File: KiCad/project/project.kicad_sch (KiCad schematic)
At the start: 27 parts, among them P1 TerminalBlock 5P 5.0mm, U1 DRV8313PWPR

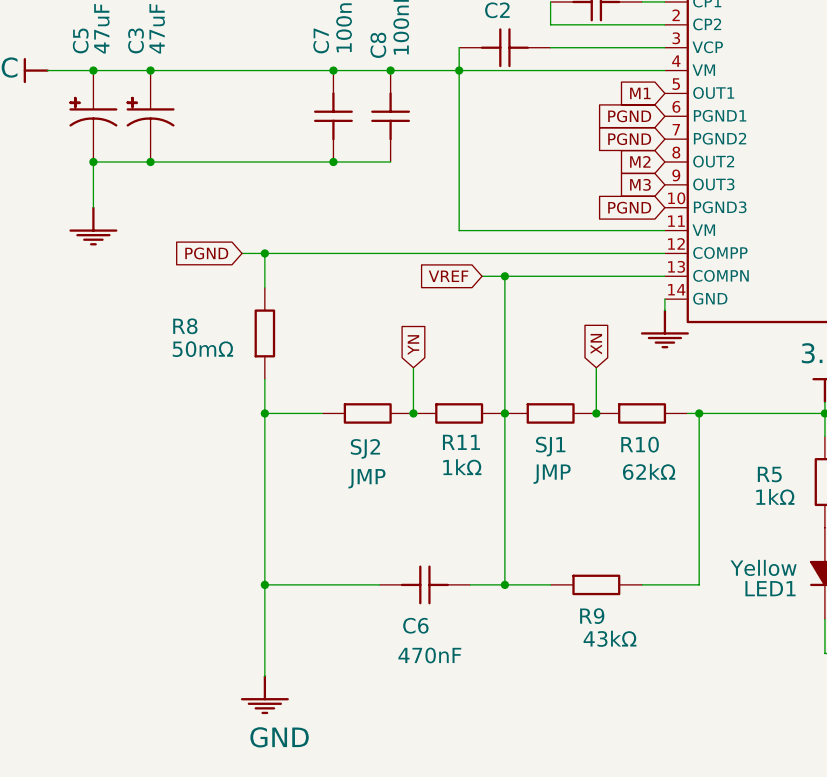
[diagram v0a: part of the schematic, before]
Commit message: Review manual layout; add power/GND/thermal improvements
Schematic: graphical-only relayout (R8/PGND-label moved, redundant GND
symbol added) — netlist verified byte-identical to prior commit; ERC 101->98.

PCB fixes & improvements:
- Re-ground U1's 8 EP thermal vias (Update-from-Schematic had stripped GND)
  and rename them to pad "29" so they survive every future sync.
- Add Power net class (0.6mm) for VCC/M1/M2/M3/PGND; widen the current-
  carrying runs 0.2->0.6mm with neck-down kept at the HTSSOP escape.
- Add F.Cu + B.Cu GND pours + 38 stitching vias (datasheet 10.1; lowers
  RthJA, better return paths/EMI).
- Extend EP thermal-via array 8->12 (6x2); add GND-return vias at the C7/C8
  VM decoupling caps.

Tooling/docs:
- check_design.py: gate hard on kicad-cli (authoritative for connectivity/
  clearance/shorts); demote KiCadRoutingTools checks to advisory (they false-
  positive on through-pad/off-anchor manual routing); re-baseline ERC to 98.
- Update CLAUDE.md + tools/README.md to match.

Verified: 0 error-severity DRC, 0 unconnected (kicad-cli), check_design PASS.
Manufacturing outputs (manufacturing/, images/) NOT regenerated — still stale.

Co-Authored-By: Claude Opus 4.8 (1M context) <noreply@anthropic.com>
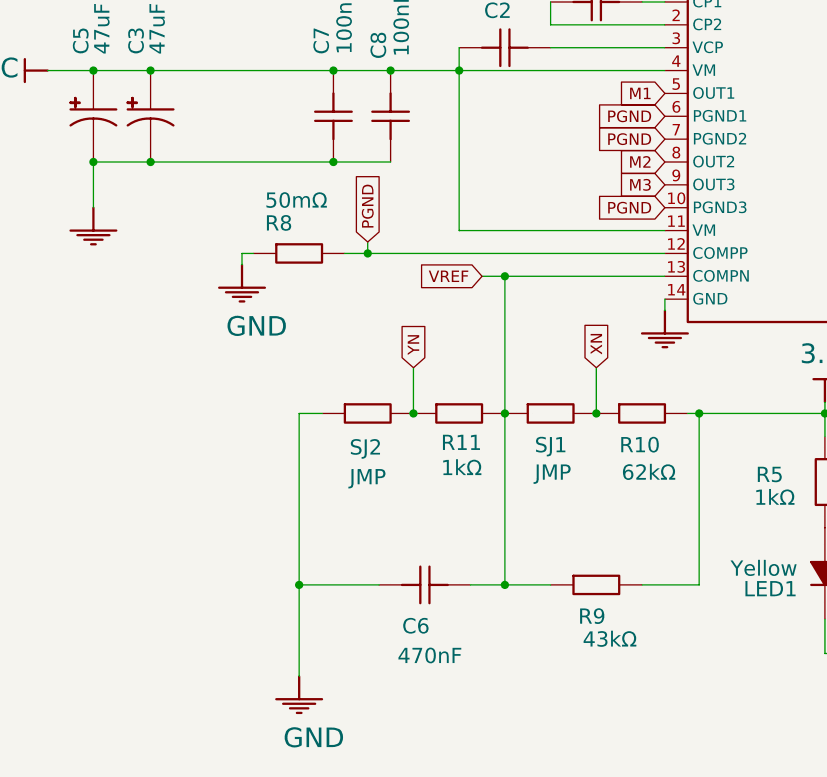
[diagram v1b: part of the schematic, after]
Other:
- moved on the sheet: R8

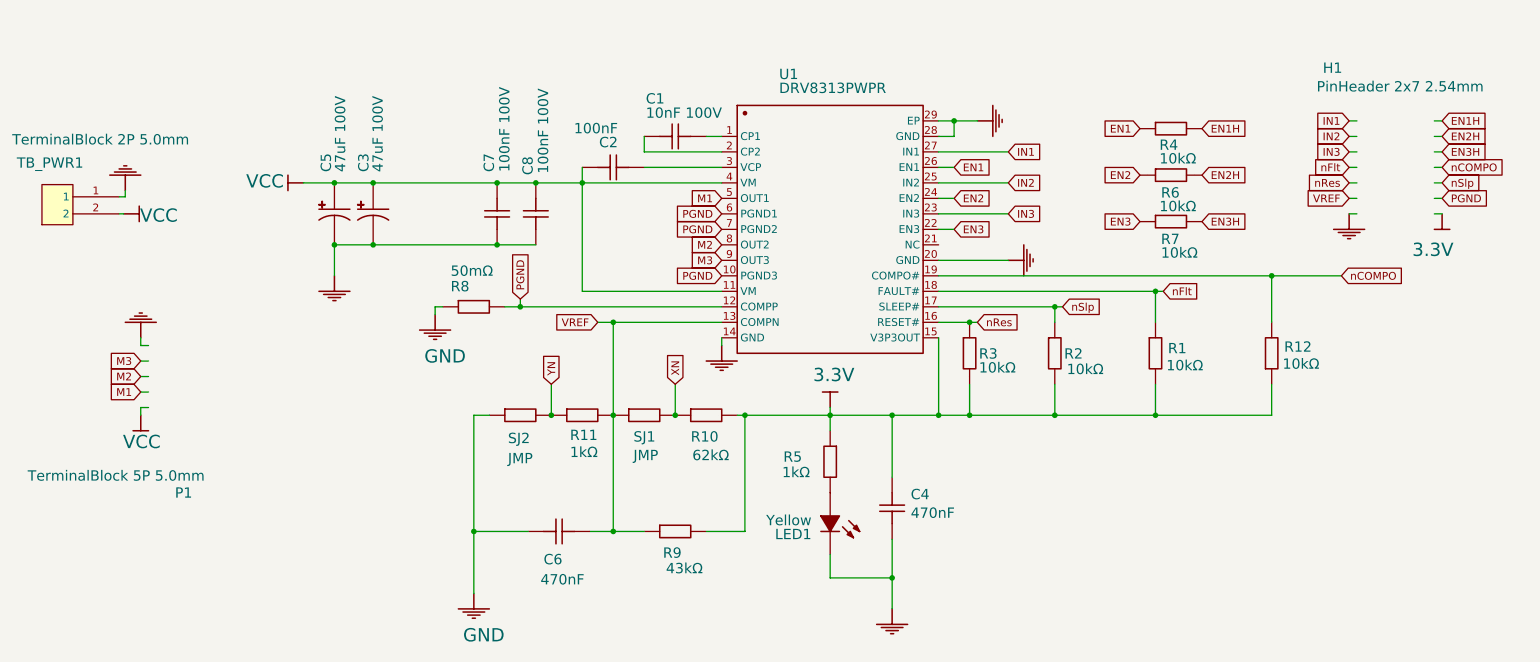
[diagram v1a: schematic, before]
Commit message: Swap simple passives to KiCad Device symbols; clear all ERC errors
Per user direction, move the simple passives off the EasyEDA-imported symbols
onto KiCad library symbols, and fix the schematic so ERC has zero errors.

- R1-R12 -> Device:R, ceramics -> Device:C, electrolytics C3/C5 ->
  Device:C_Polarized, SJ1/SJ2 -> Jumper:SolderJumper_2_Bridged. Removed the 9
  now-unused old EasyEDA passive lib_symbols. Kept U1 (no KiCad equivalent),
  H1/P1 (already generic), TB_PWR1.
- LED1 kept on its symbol (Device:LED numbers pin1=K, conflicting with the
  verified PCB pad1=anode) but its pins retyped input->passive.
- Added PWR_FLAG on VCC/GND/3.3V and a no-connect on U1.21.

Net-preserving: verified 28/28 netlist node-set parity vs the prior schematic
(re-stubbed 1.27mm where Device span 7.62 != old 10.16; jumper 10.16 exact).
kicad-skip mis-orders pin1/pin2 for some rotations, so kicad-cli netlist was
used as the oracle to detect and correct flipped parts.

ERC 98 (10 err/88 warn) -> 53 (0 err/53 warn); remaining are all import
artifacts (lib_symbol_issues/pin_to_pin/off-grid on the kept symbols).
Re-baselined check_design.py 98->53; updated tools/README.md + CLAUDE.md.
BOM unchanged; PCB untouched (only schematic.svg regenerated).

Co-Authored-By: Claude Opus 4.8 (1M context) <noreply@anthropic.com>
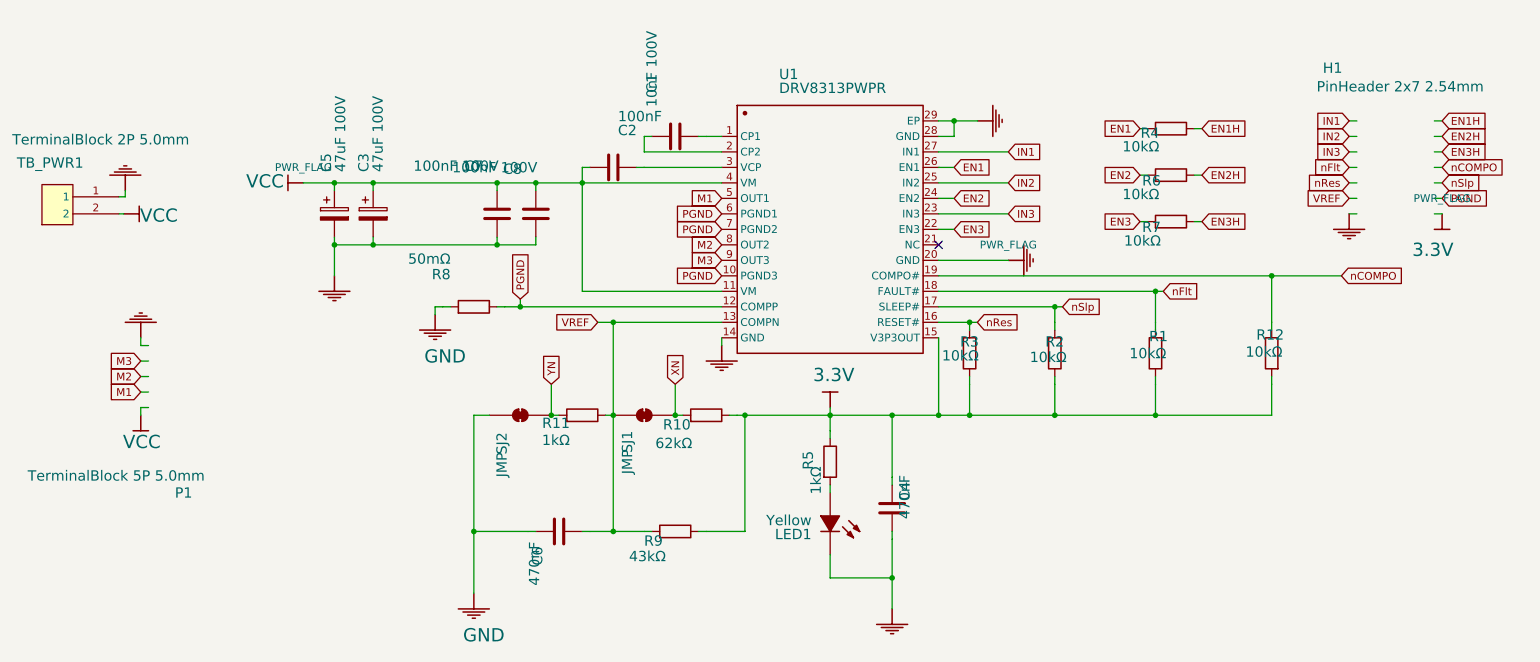
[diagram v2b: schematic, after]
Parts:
- C1: symbol CL10B104KB8NNNC -> Device:C
- C2: symbol CL10B104KB8NNNC_1 -> Device:C
- C3, C5: symbol VT1V101M-CRE77 -> Device:C_Polarized
- C4, C6, C7, C8: symbol CC0603ZRY5V6BB474 -> Device:C
- R1, R10, R11, R12, R8, R9: symbol 0603WAF4701T5E_2 -> Device:R
- R2: symbol 0603WAF4701T5E -> Device:R
- R3: symbol 0603WAF4701T5E_1 -> Device:R
- R4, R6, R7: symbol 0603WAF4701T5E_3 -> Device:R
- R5: symbol 0603WAF4701T5E_4 -> Device:R
- SJ1, SJ2: symbol 0603WAF4701T5E_2 -> Jumper:SolderJumper_2_Bridged
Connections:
- no-connect marks 0 -> 1

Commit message: Relink power symbols to KiCad power lib + type U1 pins; ERC warnings 53->8
Follow-up to the Device-symbol swap, clearing most remaining ERC warnings.

- Relinked GND/VCC/3.3V power symbols to the KiCad power library
  (power:GND / power:VCC / power:+3.3V). A power symbol's net name comes from
  its instance Value field, so the 3.3V instances keep Value 3.3V and the net
  stays 3.3V (no PCB net rename) -- verified by netlist.
- Typed U1's pins: power_in (VM/GND/EP), power_out (V3P3OUT), output (OUT1-3),
  open_collector (nFAULT/nCOMPO), passive (rest). Left IN/EN/nRESET/nSLEEP/
  COMPP/COMPN as passive on purpose -- their drivers are passive (header +
  pull-ups + shunt), so typing them input would re-add pin_not_driven errors.
- V3P3OUT now drives 3.3V, so removed the redundant 3.3V PWR_FLAG (#FLG3).
- Typed TB_PWR1's pins passive (cleared its 2 pin_to_pin).

ERC 53 (0 err/53 warn) -> 8 (0 err/8 warn). Remaining 8 = 3 lib_symbol_issues
on the kept U1/LED1/TB_PWR1 symbols (no KiCad-standard equivalent) + 5
endpoint_off_grid degenerate wires at TB_PWR1/VCC (pre-existing, in HEAD~1).
Netlist node-set parity 28/28; BOM unchanged; PCB untouched (only schematic.svg
regenerated). Re-baselined check_design.py 53->8; updated tools/README.md +
CLAUDE.md.

Co-Authored-By: Claude Opus 4.8 (1M context) <noreply@anthropic.com>
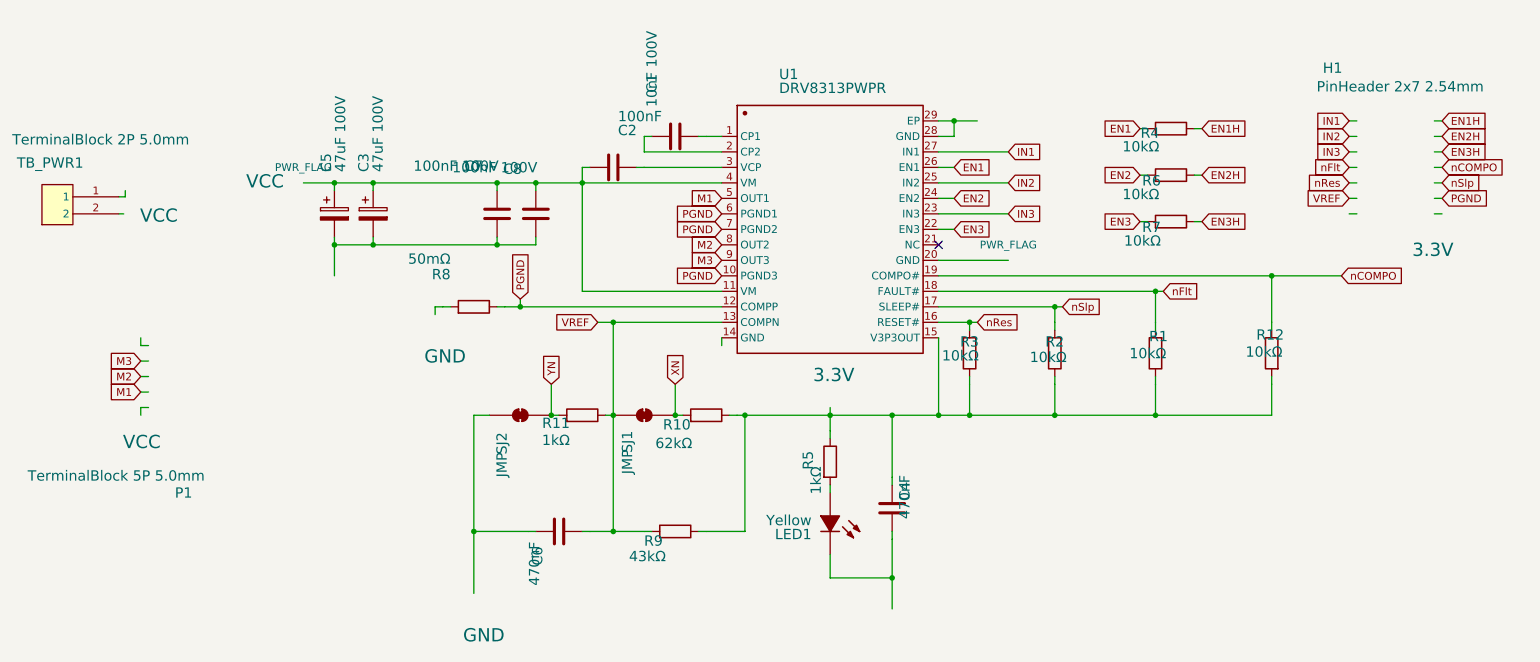
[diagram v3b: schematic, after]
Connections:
- net 3.3V: no longer names the net of C4.2, R1.1, R10.1, R12.2, R2.1, R3.1, R5.1, R9.1, U1.15 (V3P3OUT)
- removed net GND: C3.2, C4.1, C5.2, C6.2, C7.1, C8.1, LED1.2 (C), R8.2, SJ2.2 (B), TB_PWR1.1, U1.14 (GND), U1.20 (GND), U1.28 (GND), U1.29 (EP)
- net VCC: no longer names the net of C2.1, C3.1, C5.1, C7.2, C8.2, U1.11 (VM), U1.4 (VM)
- net VCC: no longer TB_PWR1.2
- new net: C3.2, C5.2, C7.1, C8.1
- new net: U1.28 (GND), U1.29 (EP)
- new net: C4.1, LED1.2 (C)
- new net: C6.2, SJ2.2 (B)
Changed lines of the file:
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@@
 	)
 	(symbol
-		(lib_id "GND")
+		(lib_id "power:GND")
 		(at 181.61 78.74 90)
 		(unit 0)
@@
 	)
 	(symbol
-		(lib_id "GND")
+		(lib_id "power:GND")
 		(at 162.56 135.89 0)
 		(unit 0)
@@
 	)
 	(symbol
-		(lib_id "3.3V")
+		(lib_id "power:+3.3V")
 		(at 252.73 71.12 0)
 		(mirror y)
@@
 	)
 	(symbol
-		(lib_id "GND")
+		(lib_id "power:GND")
 		(at 71.12 81.28 0)
 		(unit 0)
@@
 	)
 	(symbol
-		(lib_id "GND")
+		(lib_id "power:GND")
 		(at 134.62 92.71 0)
 		(unit 0)
@@
 	)
 	(symbol
-		(lib_id "VCC")
+		(lib_id "power:VCC")
 		(at 66.04 66.04 270)
 		(mirror x)
@@
 	)
 	(symbol
-		(lib_id "VCC")
+		(lib_id "power:VCC")
 		(at 36.576 71.12 90)
 		(unit 0)
@@
 	)
 	(symbol
-		(lib_id "GND")
+		(lib_id "power:GND")
 		(at 39.37 91.44 180)
 		(unit 0)
@@
 	)
 	(symbol
-		(lib_id "VCC")
+		(lib_id "power:VCC")
 		(at 39.37 104.14 0)
 		(mirror y)
@@
 	)
 	(symbol
-		(lib_id "GND")
+		(lib_id "power:GND")
 		(at 176.53 55.88 90)
 		(unit 0)
@@
 	)
 	(symbol
-		(lib_id "GND")
+		(lib_id "power:GND")
 		(at 87.63 87.63 0)
 		(unit 0)
@@
 	)
 	(symbol
-		(lib_id "GND")
+		(lib_id "power:GND")
 		(at 237.49 71.12 0)
 		(mirror y)
@@
 	)
 	(symbol
-		(lib_id "3.3V")
+		(lib_id "power:+3.3V")
 		(at 152.4 102.87 0)
 		(mirror x)
@@
 	)
 	(symbol
-		(lib_id "GND")
+		(lib_id "power:GND")
 		(at 36.83 67.31 0)
 		(mirror x)
@@
 	)
 	(symbol
-		(lib_id "GND")
+		(lib_id "power:GND")
 		(at 93.98 133.35 0)
 		(unit 0)
@@
 					(unit 0)
 				)
-			)
-		)
-	)
-	(symbol
-		(lib_id "power:PWR_FLAG")
-		(at 252.73 71.12 0)
-		(unit 0)
-		(body_style 0)
-		(exclude_from_sim no)
-		(in_bom no)
-		(on_board yes)
-		(dnp no)
-		(property "Reference" "#FLG3"
-			(at 252.73 73.66000000000001 0)
-			(hide yes)
-			(effects (font (size 1.27 1.27)))
-		)
-		(property "Value" "PWR_FLAG"
-			(at 252.73 68.58 0)
-			(effects (font (size 1.27 1.27)))
-		)
-		(property "Footprint" ""
-			(at 252.73 71.12 0)
-			(hide yes)
-			(effects (font (size 1.27 1.27)))
-		)
-		(property "Datasheet" "~"
-			(at 252.73 71.12 0)
-			(hide yes)
-			(effects (font (size 1.27 1.27)))
-		)
-		(pin "1"
-		)
-		(instances
-			(project "project"
-				(path "/03adca04-2da2-4337-bf85-1694768d6810"
-					(reference "#FLG3")
-					(unit 0)
-				)

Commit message: ERC fully clean (0): project symbol lib for U1/LED1, TB_PWR1 -> Conn_01x02
Final cleanup taking ERC from 8 warnings to 0.

- U1 (DRV8313PWPR) and LED1's symbol have no KiCad-standard equivalent, so
  added a project symbol library KiCad/project/simplefocmini.kicad_sym + a
  project sym-lib-table, renamed the cache entries to simplefocmini:<name>, and
  relinked the instances. kicad-cli sch erc reads the project sym-lib-table
  (KIPRJMOD), so these now resolve -> 2 lib_symbol_issues cleared.
- TB_PWR1: swapped the custom TB002-500-02BE symbol to the stock
  Connector_Generic:Conn_01x02 (consistent with P1=Conn_01x05 / H1=Conn_02x07),
  and rebuilt the cluster on-grid with the GND/VCC power symbols placed
  coincident with pin1/pin2 (no wires). This cleared the last lib_symbol_issue
  AND all 5 endpoint_off_grid items (degenerate off-grid wires from the earlier
  TB_PWR1 flip). pin1->GND / pin2->VCC preserved (matches PCB).

Result: ERC 0 (was 98). check_design.py PASS; ERC_BASELINE re-baselined 8->0,
so the tripwire now catches any new ERC item. Netlist node-set parity 28/28,
BOM data identical, PCB untouched (only schematic.svg regenerated).

Co-Authored-By: Claude Opus 4.8 (1M context) <noreply@anthropic.com>
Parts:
- LED1: symbol 19-213/Y2C-CQ2R2L/3T(CY) -> simplefocmini:19-213/Y2C-CQ2R2L/3T(CY)
- TB_PWR1: symbol TB002-500-02BE -> Connector_Generic:Conn_01x02
- U1: symbol DRV8313PWPR -> simplefocmini:DRV8313PWPR
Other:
- moved on the sheet: TB_PWR1
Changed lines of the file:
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@@
 	(wire
 		(pts
-			(xy 36.576 71.12) (xy 35.814 71.12)
-		)
-		(stroke
-			(width 0)
-			(type default)
-		)
-	)
-	(wire
-		(pts
 			(xy 170.18 60.96) (xy 181.61 60.96)
 		)
@@
 	(wire
 		(pts
-			(xy 35.814 68.326) (xy 36.83 68.326)
-		)
-		(stroke
-			(width 0)
-			(type default)
-		)
-	)
-	(wire
-		(pts
 			(xy 77.47 76.2) (xy 97.79 76.2)
 		)
@@
 	(wire
 		(pts
-			(xy 36.83 68.326) (xy 36.83 67.31)
-		)
-		(stroke
-			(width 0)
-			(type default)
-		)
-	)
-	(wire
-		(pts
 			(xy 71.12 76.2) (xy 77.47 76.2)
 		)
@@
 	)
 	(symbol
-		(lib_id "DRV8313PWPR")
+		(lib_id "simplefocmini:DRV8313PWPR")
 		(at 152.4 73.66 0)
 		(unit 0)
@@
 	(symbol
 		(lib_id "power:VCC")
-		(at 36.576 71.12 90)
+		(at 27.94 73.66 180)
 		(unit 0)
 		(body_style 0)
@@
 	)
 	(symbol
-		(lib_id "19-213/Y2C-CQ2R2L/3T(CY)")
+		(lib_id "simplefocmini:19-213/Y2C-CQ2R2L/3T(CY)")
 		(at 153.67 121.92 270)
 		(unit 0)
@@
 	)
 	(symbol
-		(lib_id "TB002-500-02BE")
-		(at 29.21 69.85 0)
-		(mirror x)
-		(unit 0)
-		(body_style 0)
+		(lib_id "Connector_Generic:Conn_01x02")
+		(at 33.02 71.12 0)
+		(unit 1)
+		(body_style 1)
 		(exclude_from_sim no)
 		(in_bom yes)
@@
 				(path "/03adca04-2da2-4337-bf85-1694768d6810"
 					(reference "TB_PWR1")
-					(unit 0)
+					(unit 1)
 				)
 			)
@@
 	(symbol
 		(lib_id "power:GND")
-		(at 36.83 67.31 0)
-		(mirror x)
+		(at 27.94 71.12 0)
 		(unit 0)
 		(body_style 0)
